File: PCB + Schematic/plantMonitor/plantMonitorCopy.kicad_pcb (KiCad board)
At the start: 2 copper layers, 25.7 x 126 mm, 50 parts, among them J1 FTDI, J2 AT_ISP, J3 GPIO, Q1 DMN1019USN-13, SW1 AT_RESET, SW2 Power, SW3 BUTTON1, SW4 BUTTON2, U1 ATmega328P-A, U2 Ra-01, U3 BME280, U4 TLC555xPS, Y1 8MHz

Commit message: PCB routing
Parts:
- moved H4 94.7 mm to (238.1, 59.4)
- moved H1 82.2 mm to (268.6, 59.4)
- moved H3 42.8 mm to (238.1, 110.5)
- moved H2 21.7 mm to (268.6, 110.5)
- moved C5 0.78 mm to (264.3, 73.8)
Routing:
- net +3.3V: track 35.8 -> 144.4 mm, vias 0 -> 5
- net SDA: track 2.09 -> 92.0 mm, vias 0 -> 6
- net SCL: track 2.07 -> 74.0 mm, vias 0 -> 4
- net SCK: track 0.00 -> 65.4 mm, vias 0 -> 4
- net MOSI: track 0.00 -> 57.1 mm, vias 0 -> 4
- net MISO: track 0.00 -> 56.4 mm, vias 0 -> 4
- net RESET: track 0.00 -> 46.1 mm, vias 0 -> 3
- net D2: track 0.00 -> 37.8 mm
- net RX: track 0.00 -> 37.5 mm
- net BUTTON2: track 0.00 -> 35.3 mm, vias 0 -> 2
- net BUTTON1: track 0.00 -> 34.0 mm, vias 0 -> 2
- net TX: track 0.00 -> 30.3 mm
- net SOIL: track 2.65 -> 32.5 mm, vias 0 -> 2
- net A2: track 0.00 -> 20.1 mm
- net GND: track 24.2 -> 41.1 mm, vias 4 -> 8
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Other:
- board size 25.7 x 126 mm -> 35.5 x 126 mm

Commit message: PCB routing
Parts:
- moved U3 0.83 mm to (263.4, 55.3)
- moved C10 0.69 mm to (261.4, 55.9)
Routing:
- net GND: track 41.1 -> 154.2 mm, vias 8 -> 19
- net CS: track 0.00 -> 60.1 mm, vias 0 -> 4
- net LORA_RST: track 0.00 -> 57.6 mm, vias 0 -> 4
- net A3: track 0.51 -> 56.1 mm, vias 0 -> 1
- net DIO0: track 0.00 -> 35.4 mm, vias 0 -> 1
- net A2: track 20.1 -> 42.5 mm, vias 0 -> 4
- net SDA: track 92.0 -> 82.1 mm
- net +3.3V: track 144.4 -> 152.7 mm, vias 5 -> 6
- net MISO: track 56.4 -> 59.7 mm
- net BUTTON2: track 35.3 -> 38.2 mm
- net BUTTON1: track 34.0 -> 36.4 mm
- net RESET: track 46.1 -> 48.1 mm
- net D2: track 37.8 -> 39.7 mm
- net XTAL2: track 29.9 -> 31.7 mm
- net SCL: track 74.0 -> 72.5 mm
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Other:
- outline, holes or cut-outs redrawn

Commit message: Commit
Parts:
- renumbered C11 to C1, C4 to C10, C1 to C11, C2 to C12, C12 to C13, C13 to C14, C16 to C15, C15 to C16, C14 to C17, C10 to C2, C8 to C3, C9 to C4, C7 to C6, C6 to C7, C17 to C8, C3 to C9, H4 to H1, H1 to H2, H2 to H4, J2 to J1, J1 to J2, R4 to R1, R5 to R10, R8 to R11, R7 to R12, R11 to R4, R12 to R5, R1 to R6, R9 to R7, R10 to R8, R6 to R9, SW4 to SW1, SW3 to SW2, SW1 to SW3, SW2 to SW4, U3 to U1, U1 to U3
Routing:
- net DIO0: track 35.4 -> 87.6 mm, vias 1 -> 2
- net SDA: track 82.1 -> 70.8 mm
- net SCK: track 65.5 -> 63.8 mm
- net D2: track 39.7 -> 38.5 mm
- net +3.3V: track 152.7 -> 153.8 mm
- net BUTTON1: track 36.4 -> 37.4 mm
- net RESET: track 48.1 -> 47.0 mm
- net CS: track 60.1 -> 60.9 mm
- net SCL: track 72.5 -> 71.8 mm
- net LORA_RST: track 57.6 -> 57.1 mm
- net A3: track 56.1 -> 55.6 mm
- net GND: track 154.2 -> 154.6 mm, vias 19 -> 78
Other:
- board text added: "RESET"

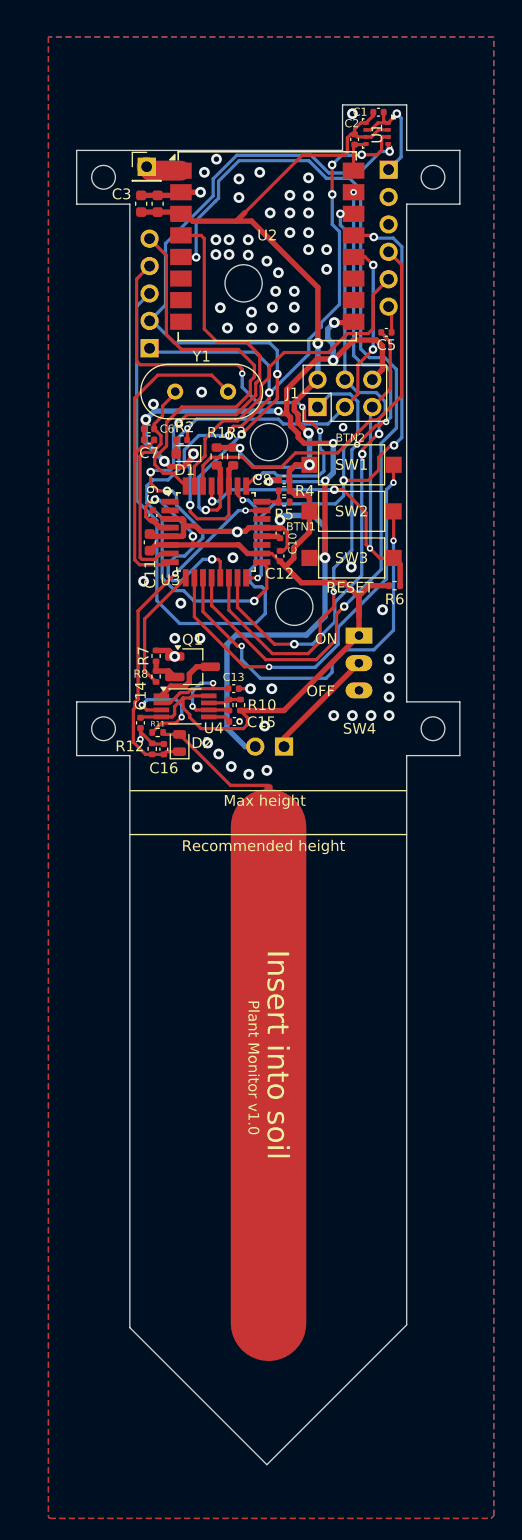
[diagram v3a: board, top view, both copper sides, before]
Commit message: Silkscreen done
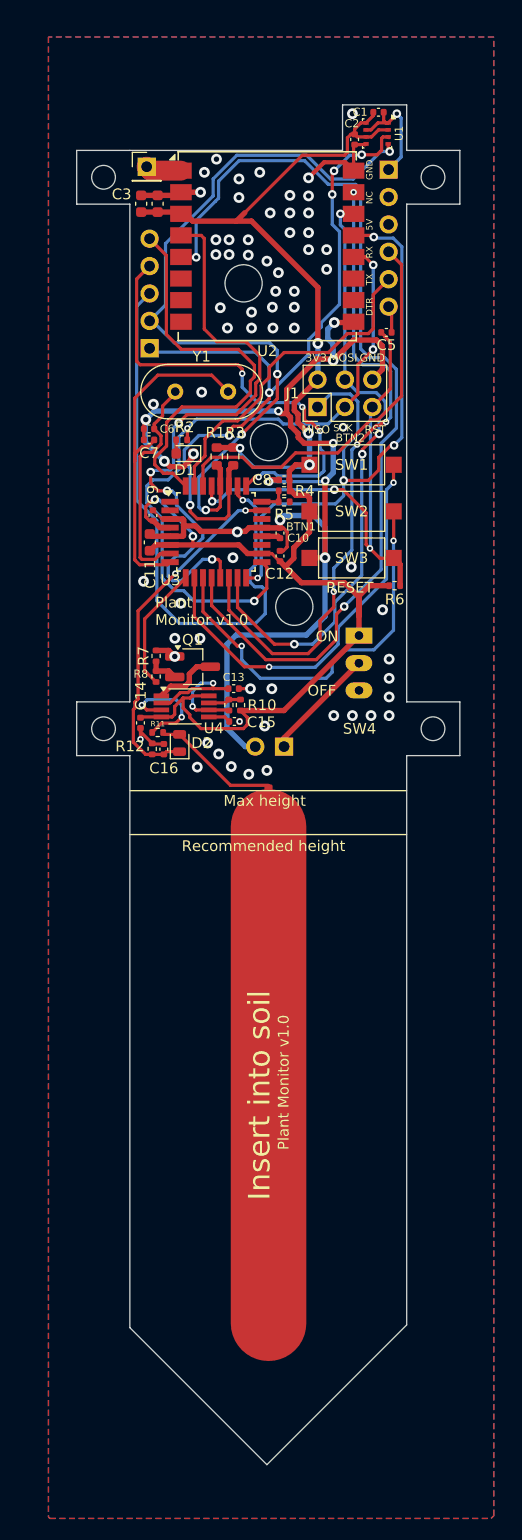
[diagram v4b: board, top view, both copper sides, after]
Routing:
- net GND: track 154.6 -> 159.7 mm
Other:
- board text added: "A2"
- board text added: "A3"
- board text added: "BUTTON1"
- board text added: "BUTTON2"
- board text added: "D2"
- board text added: "SCL"

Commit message: Part finding
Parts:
- removed U4: TLC555xPS, Package_SO:VSSOP-8_3.0x3.0mm_P0.65mm
- added U5: TLC555CDR, Package_SO:SOIC-8_3.9x4.9mm_P1.27mm, F.Cu at (234.9, 103.6)
- C13: footprint Capacitor_SMD:C_0402_1005Metric -> Capacitor_SMD:C_0603_1608Metric
- D2: value SM4007 -> MCL103A
- R8: value 10 -> 10 K
- SW3: value AT_RESET -> RESET
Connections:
- C16 pad 1: GND -> SOIL
- C16 pad 2: SOIL -> GND
